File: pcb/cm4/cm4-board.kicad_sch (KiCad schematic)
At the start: 9 parts, among them J201 Conn_01x02, J202 DF40C-100DS-0.4V_51_, J203 DF40C-100DS-0.4V_51_, U201 SN74LV1T34DBV

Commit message: update cm4 board
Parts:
- renumbered R203 to R201, R201 to R202, R202 to R203
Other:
- sheet CM4-IO ports: added ETH_GREEN, ETH_YELLOW, SD_CLK, SD_CMD, SD_DATA0, SD_DATA1, SD_DATA2, SD_DATA3, SD_PWR_ON, TRD0+, TRD0-, TRD1+, TRD1-, TRD2+, TRD2-, TRD3+, TRD3-; removed none

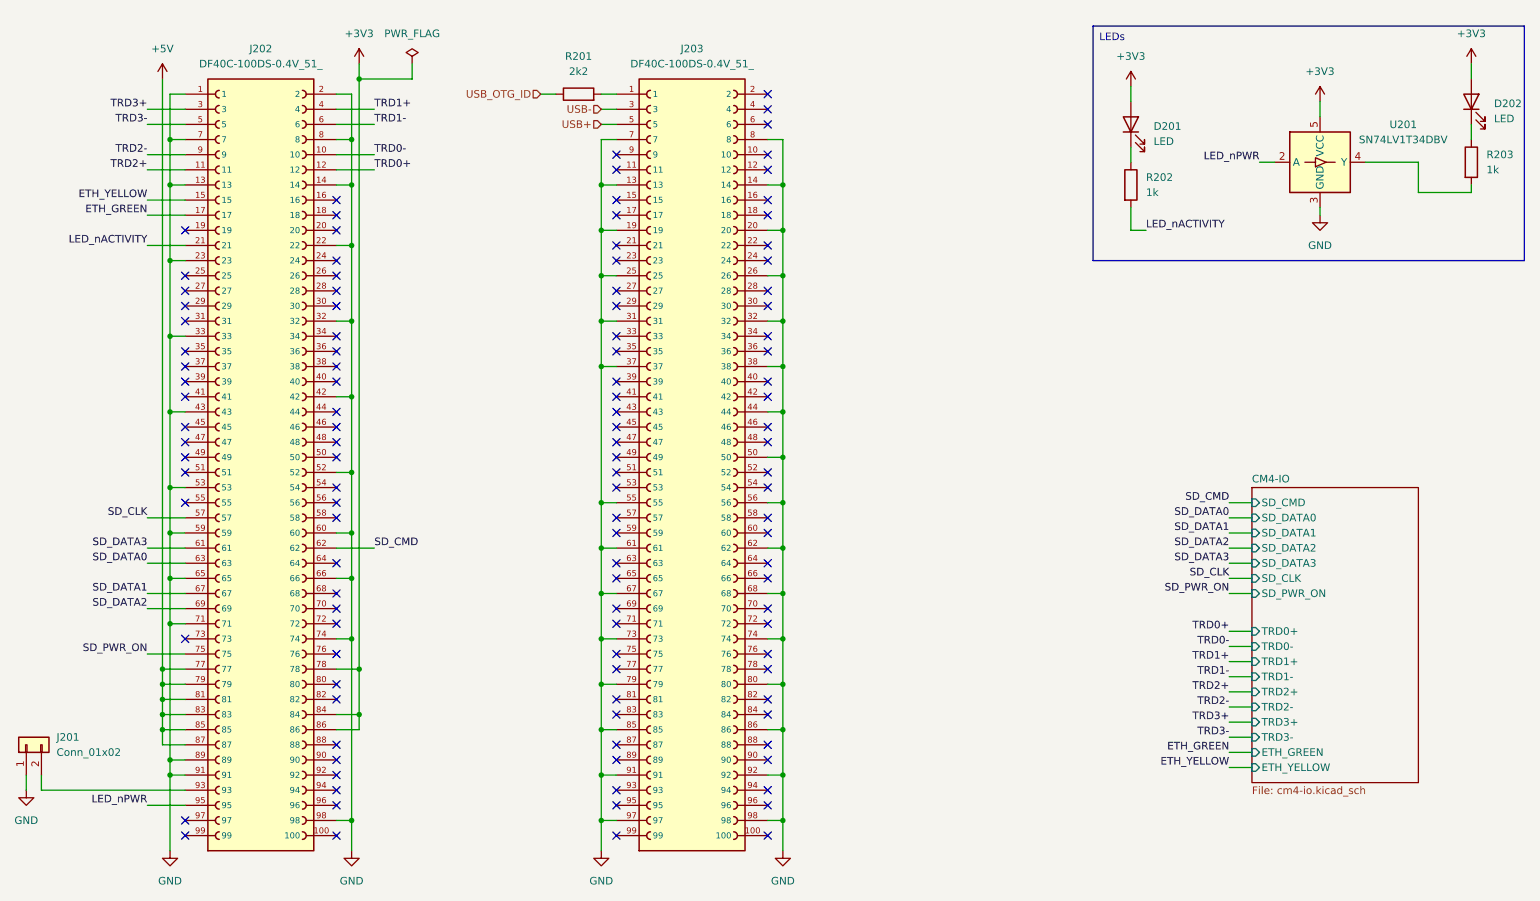
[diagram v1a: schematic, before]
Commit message: update connectors
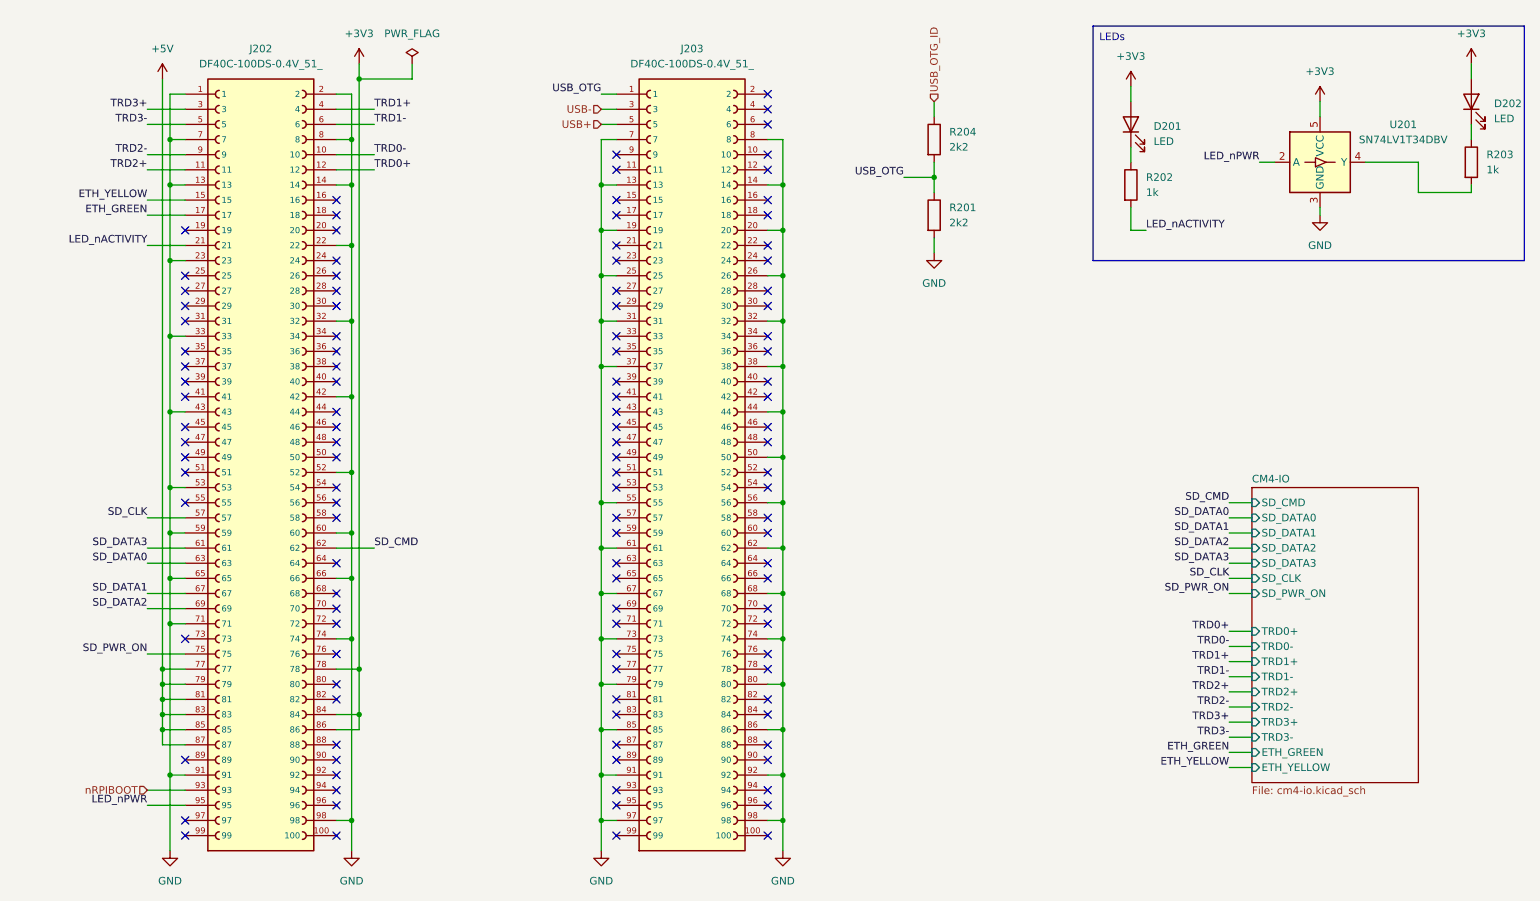
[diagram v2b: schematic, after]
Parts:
- removed J201: Conn_01x02, symbol Connector_Generic:Conn_01x02
- added R204: 2k2, symbol Device:R
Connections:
- net GND: now also R201.2; no longer J202.89
- net USB_OTG_ID: now also R204.1; no longer R201.1
- net USB_OTG: now reaches J203.1
- net USB_OTG: now also R201.1, R204.2; no longer R201.2
- net nRPIBOOT: now reaches J202.93
- no-connect marks 115 -> 116

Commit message: update cm4
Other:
- removed sheet CM4-IO
- moved on the sheet: D201, D202, R201, R202, R203, R204, U201

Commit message: update pcb
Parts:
- D201, D202: footprint (none) -> LED_SMD:LED_0805_2012Metric
- R201: renamed from R202; footprint (none) -> Resistor_SMD:R_0805_2012Metric
- R202: renamed from R204; footprint (none) -> Resistor_SMD:R_0805_2012Metric
- R203: renamed from R201; footprint (none) -> Resistor_SMD:R_0805_2012Metric
- R204: renamed from R203; footprint (none) -> Resistor_SMD:R_0805_2012Metric
- renumbered J202 to J201, J203 to J202
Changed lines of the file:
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@@
 		(dnp no)
 		(fields_autoplaced yes)
-		(property "Reference" "R203"
+		(property "Reference" "R204"
 			(at 259.08 123.1899 0)
 			(effects
@@
 			)
 		)
-		(property "Footprint" ""
+		(property "Footprint" "Resistor_SMD:R_0805_2012Metric"
 			(at 254.762 124.46 90)
 			(effects
@@
 		)
 		(property "Description" "Resistor"
+			(at 256.54 124.46 0)
+			(effects
+				(font
+					(size 1.27 1.27)
+				)
+				(hide yes)
+			)
+		)
+		(property "LCSC" ""
 			(at 256.54 124.46 0)
 			(effects
@@
 			(project "cm4"
 				(path "/5d20b266-567e-45c6-9e3e-145c2aea1daa/a64f9485-8eaf-45a8-a9d7-21ab5cb8dcb2"
-					(reference "R203")
+					(reference "R204")
 					(unit 1)
 				)
@@
 		(dnp no)
 		(fields_autoplaced yes)
-		(property "Reference" "R201"
+		(property "Reference" "R203"
 			(at 227.33 64.7699 0)
 			(effects
@@
 			)
 		)
-		(property "Footprint" ""
+		(property "Footprint" "Resistor_SMD:R_0805_2012Metric"
 			(at 223.012 66.04 90)
 			(effects
@@
 			(project "cm4"
 				(path "/5d20b266-567e-45c6-9e3e-145c2aea1daa/a64f9485-8eaf-45a8-a9d7-21ab5cb8dcb2"
-					(reference "R201")
+					(reference "R203")
 					(unit 1)
 				)
@@
 			)
 		)
-		(property "Footprint" ""
+		(property "Footprint" "LED_SMD:LED_0805_2012Metric"
 			(at 199.39 118.11 0)
 			(effects
@@
 		)
 		(property "Description" "Light emitting diode"
+			(at 199.39 118.11 0)
+			(effects
+				(font
+					(size 1.27 1.27)
+				)
+				(hide yes)
+			)
+		)
+		(property "LCSC" ""
 			(at 199.39 118.11 0)
 			(effects
@@
 		(dnp no)
 		(fields_autoplaced yes)
-		(property "Reference" "#PWR0208"
+		(property "Reference" "#PWR0207"
 			(at 199.39 115.57 0)
 			(effects
@@
 			(project "cm4"
 				(path "/5d20b266-567e-45c6-9e3e-145c2aea1daa/a64f9485-8eaf-45a8-a9d7-21ab5cb8dcb2"
-					(reference "#PWR0208")
+					(reference "#PWR0207")
 					(unit 1)
 				)
@@
 		(dnp no)
 		(fields_autoplaced yes)
-		(property "Reference" "J202"
+		(property "Reference" "J201"
 			(at 66.04 24.13 0)
 			(effects
@@
 			(project "cm4"
 				(path "/5d20b266-567e-45c6-9e3e-145c2aea1daa/a64f9485-8eaf-45a8-a9d7-21ab5cb8dcb2"
-					(reference "J202")
+					(reference "J201")
 					(unit 1)
 				)
@@
 		(dnp no)
 		(fields_autoplaced yes)
-		(property "Reference" "#PWR0203"
+		(property "Reference" "#PWR0202"
 			(at 50.8 165.1 0)
 			(effects
@@
 			(project "cm4"
 				(path "/5d20b266-567e-45c6-9e3e-145c2aea1daa/a64f9485-8eaf-45a8-a9d7-21ab5cb8dcb2"
-					(reference "#PWR0203")
+					(reference "#PWR0202")
 					(unit 1)
 				)
@@
 		(dnp no)
 		(fields_autoplaced yes)
-		(property "Reference" "R202"
+		(property "Reference" "R201"
 			(at 201.93 126.9999 0)
 			(effects
@@
 			)
 		)
-		(property "Footprint" ""
+		(property "Footprint" "Resistor_SMD:R_0805_2012Metric"
 			(at 197.612 128.27 90)
 			(effects
@@
 		)
 		(property "Description" "Resistor"
+			(at 199.39 128.27 0)
+			(effects
+				(font
+					(size 1.27 1.27)
+				)
+				(hide yes)
+			)
+		)
+		(property "LCSC" ""
 			(at 199.39 128.27 0)
 			(effects
@@
 			(project "cm4"
 				(path "/5d20b266-567e-45c6-9e3e-145c2aea1daa/a64f9485-8eaf-45a8-a9d7-21ab5cb8dcb2"
-					(reference "R202")
+					(reference "R201")
 					(unit 1)
 				)
@@
 		(dnp no)
 		(fields_autoplaced yes)
-		(property "Reference" "#PWR0205"
+		(property "Reference" "#PWR0204"
 			(at 82.55 30.48 0)
 			(effects
@@
 			(project ""
 				(path "/5d20b266-567e-45c6-9e3e-145c2aea1daa/a64f9485-8eaf-45a8-a9d7-21ab5cb8dcb2"
-					(reference "#PWR0205")
+					(reference "#PWR0204")
 					(unit 1)
 				)
@@
 		(dnp no)
 		(fields_autoplaced yes)
-		(property "Reference" "#PWR0202"
+		(property "Reference" "#PWR0201"
 			(at 49.53 33.02 0)
 			(effects
@@
 			(project ""
 				(path "/5d20b266-567e-45c6-9e3e-145c2aea1daa/a64f9485-8eaf-45a8-a9d7-21ab5cb8dcb2"
-					(reference "#PWR0202")
+					(reference "#PWR0201")
 					(unit 1)
 				)
@@
 		(dnp no)
 		(fields_autoplaced yes)
-		(property "Reference" "#PWR0206"
+		(property "Reference" "#PWR0205"
 			(at 123.19 165.1 0)
 			(effects
@@
 			(project "cm4"
 				(path "/5d20b266-567e-45c6-9e3e-145c2aea1daa/a64f9485-8eaf-45a8-a9d7-21ab5cb8dcb2"
-					(reference "#PWR0206")
+					(reference "#PWR0205")
 					(unit 1)
 				)
@@
 		(dnp no)
 		(fields_autoplaced yes)
-		(property "Reference" "J203"
+		(property "Reference" "J202"
 			(at 138.43 24.13 0)
 			(effects
@@
 			(project "cm4"
 				(path "/5d20b266-567e-45c6-9e3e-145c2aea1daa/a64f9485-8eaf-45a8-a9d7-21ab5cb8dcb2"
-					(reference "J203")
+					(reference "J202")
 					(unit 1)
 				)
@@
 		(dnp no)
 		(fields_autoplaced yes)
-		(property "Reference" "#PWR0207"
+		(property "Reference" "#PWR0206"
 			(at 153.67 165.1 0)
 			(effects
@@
 			(project "cm4"
 				(path "/5d20b266-567e-45c6-9e3e-145c2aea1daa/a64f9485-8eaf-45a8-a9d7-21ab5cb8dcb2"
-					(reference "#PWR0207")
+					(reference "#PWR0206")
 					(unit 1)
 				)
@@
 		(dnp no)
 		(fields_autoplaced yes)
-		(property "Reference" "#PWR0204"
+		(property "Reference" "#PWR0203"
 			(at 81.28 165.1 0)
 			(effects
@@
 			(project "cm4"
 				(path "/5d20b266-567e-45c6-9e3e-145c2aea1daa/a64f9485-8eaf-45a8-a9d7-21ab5cb8dcb2"
-					(reference "#PWR0204")
+					(reference "#PWR0203")
 					(unit 1)
 				)
@@
 		(dnp no)
 		(fields_autoplaced yes)
-		(property "Reference" "#PWR0201"
+		(property "Reference" "#PWR0208"
 			(at 224.79 78.74 0)
 			(effects
@@
 			(project "cm4"
 				(path "/5d20b266-567e-45c6-9e3e-145c2aea1daa/a64f9485-8eaf-45a8-a9d7-21ab5cb8dcb2"
-					(reference "#PWR0201")
+					(reference "#PWR0208")
 					(unit 1)
 				)
@@
 		(dnp no)
 		(fields_autoplaced yes)
-		(property "Reference" "R204"
+		(property "Reference" "R202"
 			(at 227.33 52.0699 0)
 			(effects
@@
 			)
 		)
-		(property "Footprint" ""
+		(property "Footprint" "Resistor_SMD:R_0805_2012Metric"
 			(at 223.012 53.34 90)
 			(effects
@@
 			(project "cm4"
 				(path "/5d20b266-567e-45c6-9e3e-145c2aea1daa/a64f9485-8eaf-45a8-a9d7-21ab5cb8dcb2"
-					(reference "R204")
+					(reference "R202")
 					(unit 1)
 				)
@@
 			)
 		)
-		(property "Footprint" ""
+		(property "Footprint" "LED_SMD:LED_0805_2012Metric"
 			(at 256.54 114.3 0)
 			(effects
@@
 			(at 256.54 114.3 0)
 			(effects
+				(font
+					(size 1.27 1.27)
+				)
+				(hide yes)
+			)
+		)
+		(property "LCSC" ""
+			(at 256.54 114.3 0)
+			(effects

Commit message: update parts
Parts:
- J201, J202: Availability In Stock -> (none); Check_prices https://www.snapeda.com/parts/DF40C-100DS-0.4V(51)/Hirose/v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 -> (none); Description_1 100 Position Connector Receptacle, Center Strip Contacts Su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 -> (none); MANUFACTURER Hirose -> (none); MAXIMUM_PACKAGE_HEIGHT 1.65mm -> (none); MF Hirose -> (none); MP DF40C-100DS-0.4V(51) -> (none); PARTREV Oct.1.2023 -> (none); Package None -> (none); Price None -> (none); STANDARD Manufacturer Recommendations -> (none); SnapEDA_Link https://www.snapeda.com/parts/DF40C-100DS-0.4V(51)/Hirose/v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 -> (none)

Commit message: update cm4 board
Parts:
- J201, J202: LCSC (none) -> C597931
- U201: LCSC (none) -> C100024
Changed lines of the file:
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@@
 			)
 		)
-		(property "LCSC" ""
+		(property "LCSC" "C597931"
 			(at 66.04 92.71 0)
 			(effects
@@
 			)
 		)
+		(property "LCSC" "C100024"
+			(at 231.14 124.46 0)
+			(effects
+				(font
+					(size 1.27 1.27)
+				)
+				(hide yes)
+			)
+		)
 		(pin "4"
 		)
@@
 			)
 		)
-		(property "LCSC" ""
+		(property "LCSC" "C597931"
 			(at 138.43 92.71 0)
 			(effects

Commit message: cm4: update footprint library, add 3d files, update dimensions
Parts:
- J201, J202: footprint DF40C-100DS-0.4V_51_:HIROSE_DF40C-100DS-0.4V_51_ -> PRJ:HIROSE_DF40C-100DS-0.4V_51_
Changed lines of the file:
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@@
 	(label "USB_OTG"
 		(at 123.19 31.75 180)
-		(fields_autoplaced yes)
 		(effects
 			(font
@@
 	(label "LED_nPWR"
 		(at 46.99 151.13 180)
-		(fields_autoplaced yes)
 		(effects
 			(font
@@
 	(label "LED_nACTIVITY"
 		(at 46.99 57.15 180)
-		(fields_autoplaced yes)
 		(effects
 			(font
@@
 	(label "LED_nACTIVITY"
 		(at 201.93 135.89 0)
-		(fields_autoplaced yes)
 		(effects
 			(font
@@
 	(label "USB_OTG"
 		(at 219.71 59.69 180)
-		(fields_autoplaced yes)
 		(effects
 			(font
@@
 	(label "LED_nPWR"
 		(at 220.98 124.46 180)
-		(fields_autoplaced yes)
 		(effects
 			(font
@@
 		(shape input)
 		(at 46.99 44.45 180)
-		(fields_autoplaced yes)
 		(effects
 			(font
@@
 		(shape input)
 		(at 123.19 34.29 180)
-		(fields_autoplaced yes)
 		(effects
 			(font
@@
 		(shape input)
 		(at 46.99 148.59 180)
-		(fields_autoplaced yes)
 		(effects
 			(font
@@
 		(shape input)
 		(at 123.19 36.83 180)
-		(fields_autoplaced yes)
 		(effects
 			(font
@@
 		(shape input)
 		(at 85.09 36.83 0)
-		(fields_autoplaced yes)
 		(effects
 			(font
@@
 		(shape input)
 		(at 224.79 46.99 90)
-		(fields_autoplaced yes)
 		(effects
 			(font
@@
 		(shape input)
 		(at 46.99 41.91 180)
-		(fields_autoplaced yes)
 		(effects
 			(font
@@
 		(shape input)
 		(at 85.09 34.29 0)
-		(fields_autoplaced yes)
 		(effects
 			(font
@@
 		(shape input)
 		(at 85.09 41.91 0)
-		(fields_autoplaced yes)
 		(effects
 			(font
@@
 		(shape input)
 		(at 46.99 125.73 180)
-		(fields_autoplaced yes)
 		(effects
 			(font
@@
 		(shape input)
 		(at 85.09 44.45 0)
-		(fields_autoplaced yes)
 		(effects
 			(font
@@
 		(shape input)
 		(at 46.99 102.87 180)
-		(fields_autoplaced yes)
 		(effects
 			(font
@@
 		(shape input)
 		(at 46.99 118.11 180)
-		(fields_autoplaced yes)
 		(effects
 			(font
@@
 		(shape input)
 		(at 46.99 49.53 180)
-		(fields_autoplaced yes)
 		(effects
 			(font
@@
 		(shape input)
 		(at 46.99 34.29 180)
-		(fields_autoplaced yes)
 		(effects
 			(font
@@
 		(shape input)
 		(at 46.99 36.83 180)
-		(fields_autoplaced yes)
 		(effects
 			(font
@@
 		(shape input)
 		(at 46.99 115.57 180)
-		(fields_autoplaced yes)
 		(effects
 			(font
@@
 		(shape input)
 		(at 46.99 52.07 180)
-		(fields_autoplaced yes)
 		(effects
 			(font
@@
 		(shape input)
 		(at 46.99 107.95 180)
-		(fields_autoplaced yes)
 		(effects
 			(font
@@
 		(shape input)
 		(at 46.99 110.49 180)
-		(fields_autoplaced yes)
 		(effects
 			(font
@@
 		(shape input)
 		(at 85.09 107.95 0)
-		(fields_autoplaced yes)
 		(effects
 			(font
@@
 			)
 		)
-		(property "Footprint" "DF40C-100DS-0.4V_51_:HIROSE_DF40C-100DS-0.4V_51_"
+		(property "Footprint" "PRJ:HIROSE_DF40C-100DS-0.4V_51_"
 			(at 66.04 92.71 0)
 			(effects
@@
 			)
 		)
-		(property "Footprint" "DF40C-100DS-0.4V_51_:HIROSE_DF40C-100DS-0.4V_51_"
+		(property "Footprint" "PRJ:HIROSE_DF40C-100DS-0.4V_51_"
 			(at 138.43 92.71 0)
 			(effects
